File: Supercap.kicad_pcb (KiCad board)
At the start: 4 copper layers, 151.8 x 70 mm, 73 parts, among them IC1 NCP5109ADR2G, IC2 NCP5109ADR2G, J1 XT30, J2 XT30, J2-J1 Conn_01x10, J3 Conn_01x01, J3-J1 Conn_01x10, J4 Conn_01x01, P7803B-1000R1 P7803B-1000, P7812B-1000R1 490-P7812B-1000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

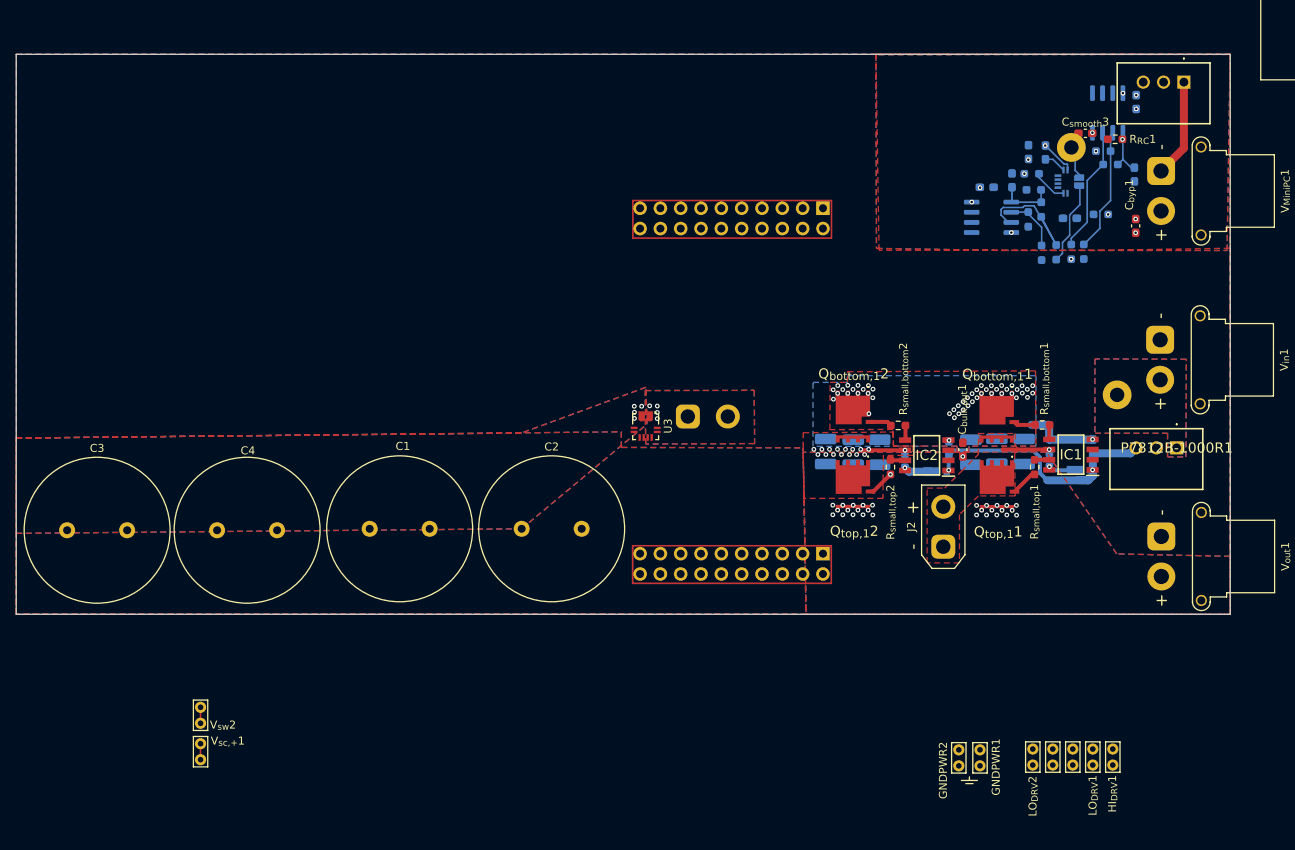
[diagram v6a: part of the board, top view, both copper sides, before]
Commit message: finished foundation pours, layout, tp routing along edges. Next: cursed routing I sense IC/H to 3v3, 3v3 to mspm0
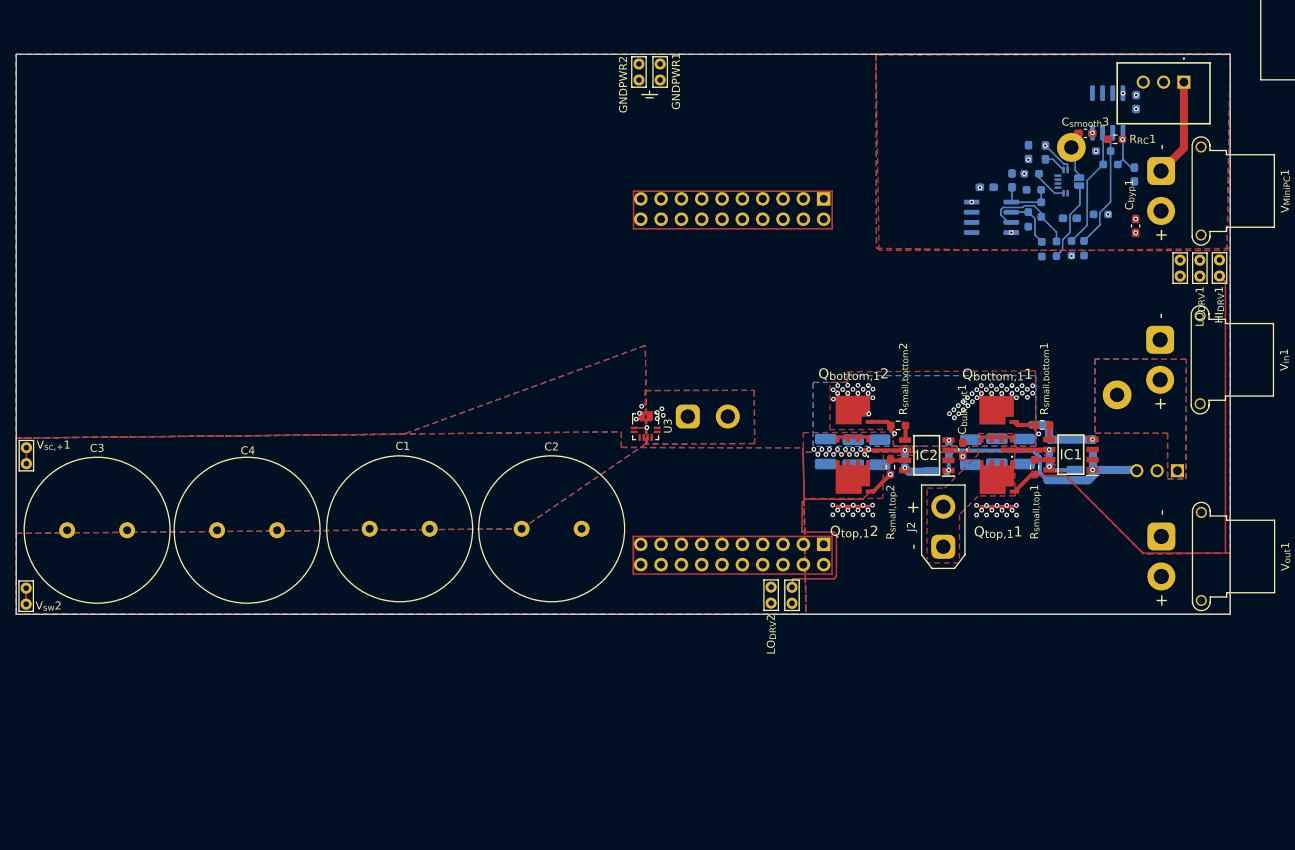
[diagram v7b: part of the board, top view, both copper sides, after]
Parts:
- P7812B-1000R1: moved to B.Cu
- moved GNDPWR1 94.6 mm to (118.1, 74.5)
- moved GNDPWR2 94.6 mm to (115.4, 74.5)
- moved V_{sw}1 62.6 mm to (183.1, 99.0)
- moved HI_{DRV}1 62.6 mm to (188.0, 99.0)
- moved LO_{DRV}1 62.6 mm to (185.5, 99.0)
- moved V_{sc,+}1 42.9 mm to (38.8, 122.5)
- moved HI_{DRV}2 39.5 mm to (134.5, 137.9), turned to -90 degrees
- moved LO_{DRV}2 38.5 mm to (131.9, 139.9)
- moved V_{sw}2 26.4 mm to (38.8, 140.0)
- moved P7812B-1000R1 2.86 mm to (182.7, 123.3)
- moved J3-J1 1.17 mm to (138.5, 89.3)
- moved J2-J1 1.17 mm to (138.5, 132.5)
- moved R1 0.45 mm to (169.5, 95.5)
- moved R_{sens,top}1 0.45 mm to (167.6, 95.6)
- moved R_{sens,top}2 0.45 mm to (165.8, 95.6)
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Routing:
- net /Voltage Converter/LO_DRV_{1}: track 4.73 -> 73.5 mm, vias 0 -> 1
- net /Voltage Converter/V_{sw,1}: track 7.83 -> 75.2 mm
- net /Voltage Converter/HI_DRV_{1}: track 5.47 -> 68.4 mm
- net /Voltage Converter/LO_DRV_{2}: track 4.73 -> 51.4 mm, vias 0 -> 1
- net GND: track 0.00 -> 45.8 mm, vias 5 -> 6
- net /Voltage Converter/HI_DRV_{2}: track 8.00 -> 37.2 mm
- net Net-(U2A-+): track 16.3 -> 12.3 mm
- net /Control/V_{sc,+}: vias 5 -> 4

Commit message: that took a lot longer than i thought and so cursed. looks kinda cool though, finished the H bridge/3v3/mspm0 traces, tried to keep along edges. holding off on via stitching just yet cuz im sure glorious leader egan will have interesting things to say about my choices :)
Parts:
- moved R_{pu}1 19.8 mm to (153.4, 91.6)
- moved C_{l}1 16.1 mm to (153.3, 89.7), turned to 180 degrees
- moved R_{RC}2 7.99 mm to (157.7, 84.5)
- moved C_{byp}2 3.57 mm to (164.5, 79.9)
- moved C_{RC}2 1.81 mm to (162.0, 85.2)
- moved C_{d2}1 0.13 mm to (160.2, 121.0)
- moved C_{d1}1 0.12 mm to (163.5, 121.0)
- moved C_{bulk,out}1 0.10 mm to (156.0, 120.6)
- moved C_{d3}1 0.10 mm to (138.8, 121.0)
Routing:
- net /Control/PA8: track 0.41 -> 97.2 mm, vias 0 -> 3
- net /Control/PA22: track 0.41 -> 92.1 mm, vias 0 -> 5
- net /Control/PA25: track 0.44 -> 91.3 mm, vias 0 -> 3
- net /Control/I_{bat,out+}: track 10.0 -> 100.3 mm, vias 29 -> 31
- net /Control/PB9: track 0.44 -> 87.9 mm, vias 0 -> 2
- net /Control/I_L: track 0.00 -> 84.4 mm, vias 0 -> 3
- net /Voltage Converter/V_{sw,2}: track 7.37 -> 83.0 mm, vias 16 -> 9
- net /Control/PA15: track 0.00 -> 74.2 mm, vias 0 -> 2
- net /Control/V_{sc,+}: track 2.00 -> 75.9 mm, vias 4 -> 3
- net /Control/+3V3: track 4.42 -> 72.6 mm, vias 9 -> 11
- net /Control/F_L: track 0.00 -> 63.3 mm, vias 0 -> 3
- net /Control/F_bat: track 4.35 -> 63.3 mm, vias 0 -> 2
- net /Control/I_bat: track 2.81 -> 55.6 mm, vias 0 -> 1
- net /Control/PA16: track 0.00 -> 50.7 mm, vias 0 -> 2
- net GNDPWR: track 16.9 -> 3.97 mm
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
